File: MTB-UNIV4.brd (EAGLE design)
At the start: 106 x 67 mm, 138 parts, among them IC1 MEGA128-A, IC2 SN75176BP, IC3 MC7805CDTG, IC4 ULN2803A, IC5 ULN2803A, X1 CON-04-5.0CON-5MM, X2 CON-04-5.0CON-5MM, X3 1751316, X4 1751316, X5 1751316, X6 1751316

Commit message: Do not ground mount holes.
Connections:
- net GND: no longer H1.B3,2, H2.B3,2, H3.B3,2, H4.B3,2
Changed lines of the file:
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@@
 <?xml version="1.0" encoding="utf-8"?>
 <!DOCTYPE eagle SYSTEM "eagle.dtd">
-<eagle version="9.6.2">
+<eagle version="9.5.2">
 <drawing>
 <settings>
@@
 <setting verticaltext="up"/>
 </settings>
-<grid distance="0.5" unitdist="mm" unit="mm" style="lines" multiple="1" display="yes" altdistance="5" altunitdist="mil" altunit="mil"/>
+<grid distance="1.27" unitdist="mm" unit="mm" style="dots" multiple="2" display="no" altdistance="0.3175" altunitdist="mm" altunit="mm"/>
 <layers>
-<layer number="1" name="Top" color="4" fill="1" visible="yes" active="yes"/>
+<layer number="1" name="Top" color="3" fill="1" visible="yes" active="yes"/>
 <layer number="2" name="Route2" color="1" fill="3" visible="no" active="no"/>
 <layer number="3" name="Route3" color="4" fill="3" visible="no" active="no"/>
@@
 <layer number="14" name="Route14" color="1" fill="6" visible="no" active="no"/>
 <layer number="15" name="Route15" color="4" fill="6" visible="no" active="no"/>
-<layer number="16" name="Bottom" color="1" fill="1" visible="yes" active="yes"/>
+<layer number="16" name="Bottom" color="4" fill="1" visible="yes" active="yes"/>
 <layer number="17" name="Pads" color="2" fill="1" visible="yes" active="yes"/>
 <layer number="18" name="Vias" color="2" fill="1" visible="yes" active="yes"/>
@@
 <layer number="23" name="tOrigins" color="15" fill="1" visible="yes" active="yes"/>
 <layer number="24" name="bOrigins" color="15" fill="1" visible="yes" active="yes"/>
-<layer number="25" name="tNames" color="7" fill="1" visible="yes" active="yes"/>
-<layer number="26" name="bNames" color="7" fill="1" visible="yes" active="yes"/>
-<layer number="27" name="tValues" color="7" fill="1" visible="yes" active="yes"/>
+<layer number="25" name="tNames" color="7" fill="1" visible="no" active="yes"/>
+<layer number="26" name="bNames" color="7" fill="1" visible="no" active="yes"/>
+<layer number="27" name="tValues" color="7" fill="1" visible="no" active="yes"/>
 <layer number="28" name="bValues" color="7" fill="1" visible="no" active="yes"/>
 <layer number="29" name="tStop" color="7" fill="3" visible="no" active="yes"/>
@@
 <layer number="37" name="tTest" color="7" fill="1" visible="no" active="yes"/>
 <layer number="38" name="bTest" color="7" fill="1" visible="no" active="yes"/>
-<layer number="39" name="tKeepout" color="4" fill="11" visible="yes" active="yes"/>
-<layer number="40" name="bKeepout" color="1" fill="11" visible="yes" active="yes"/>
-<layer number="41" name="tRestrict" color="4" fill="10" visible="yes" active="yes"/>
-<layer number="42" name="bRestrict" color="1" fill="10" visible="yes" active="yes"/>
-<layer number="43" name="vRestrict" color="2" fill="10" visible="yes" active="yes"/>
+<layer number="39" name="tKeepout" color="4" fill="11" visible="no" active="yes"/>
+<layer number="40" name="bKeepout" color="1" fill="11" visible="no" active="yes"/>
+<layer number="41" name="tRestrict" color="4" fill="10" visible="no" active="yes"/>
+<layer number="42" name="bRestrict" color="1" fill="10" visible="no" active="yes"/>
+<layer number="43" name="vRestrict" color="2" fill="10" visible="no" active="yes"/>
 <layer number="44" name="Drills" color="7" fill="1" visible="no" active="yes"/>
-<layer number="45" name="Holes" color="7" fill="1" visible="yes" active="yes"/>
-<layer number="46" name="Milling" color="3" fill="1" visible="no" active="yes"/>
+<layer number="45" name="Holes" color="7" fill="1" visible="no" active="yes"/>
+<layer number="46" name="Milling" color="3" fill="1" visible="yes" active="yes"/>
 <layer number="47" name="Measures" color="7" fill="1" visible="no" active="yes"/>
-<layer number="48" name="Document" color="7" fill="1" visible="yes" active="yes"/>
+<layer number="48" name="Document" color="7" fill="1" visible="no" active="yes"/>
 <layer number="49" name="Reference" color="7" fill="1" visible="yes" active="yes"/>
 <layer number="50" name="dxf" color="7" fill="1" visible="no" active="yes"/>
@@
 <layer number="112" name="tSilk" color="7" fill="1" visible="no" active="yes"/>
 <layer number="113" name="ReferenceLS" color="7" fill="1" visible="no" active="no"/>
-<layer number="114" name="Badge_Outline" color="7" fill="1" visible="yes" active="yes"/>
-<layer number="115" name="ReferenceISLANDS" color="7" fill="1" visible="yes" active="yes"/>
-<layer number="116" name="Patch_BOT" color="9" fill="4" visible="no" active="yes"/>
+<layer number="114" name="Badge_Outline" color="7" fill="1" visible="no" active="yes"/>
+<layer number="115" name="ReferenceISLANDS" color="7" fill="1" visible="no" active="yes"/>
+<layer number="116" name="centerDrill" color="9" fill="4" visible="no" active="yes"/>
 <layer number="118" name="Rect_Pads" color="7" fill="1" visible="no" active="no"/>
 <layer number="121" name="_tsilk" color="7" fill="1" visible="no" active="yes"/>
@@
 <layer number="127" name="_tValues" color="7" fill="1" visible="no" active="yes"/>
 <layer number="128" name="_bValues" color="7" fill="1" visible="no" active="yes"/>
-<layer number="129" name="Mask" color="7" fill="1" visible="yes" active="yes"/>
+<layer number="129" name="Mask" color="7" fill="1" visible="no" active="yes"/>
 <layer number="131" name="tAdjust" color="7" fill="1" visible="no" active="yes"/>
 <layer number="132" name="bAdjust" color="7" fill="1" visible="no" active="yes"/>
@@
 <layer number="223" name="223bmp" color="24" fill="1" visible="no" active="no"/>
 <layer number="224" name="224bmp" color="25" fill="1" visible="no" active="no"/>
-<layer number="225" name="225bmp" color="7" fill="1" visible="yes" active="yes"/>
-<layer number="226" name="226bmp" color="7" fill="1" visible="yes" active="yes"/>
-<layer number="227" name="227bmp" color="7" fill="1" visible="yes" active="yes"/>
-<layer number="228" name="228bmp" color="7" fill="1" visible="yes" active="yes"/>
-<layer number="229" name="229bmp" color="7" fill="1" visible="yes" active="yes"/>
-<layer number="230" name="230bmp" color="7" fill="1" visible="yes" active="yes"/>
+<layer number="225" name="225bmp" color="7" fill="1" visible="no" active="yes"/>
+<layer number="226" name="226bmp" color="7" fill="1" visible="no" active="yes"/>
+<layer number="227" name="227bmp" color="7" fill="1" visible="no" active="yes"/>
+<layer number="228" name="228bmp" color="7" fill="1" visible="no" active="yes"/>
+<layer number="229" name="229bmp" color="7" fill="1" visible="no" active="yes"/>
+<layer number="230" name="230bmp" color="7" fill="1" visible="no" active="yes"/>
 <layer number="231" name="Eagle3D_PG1" color="7" fill="1" visible="no" active="no"/>
 <layer number="232" name="Eagle3D_PG2" color="7" fill="1" visible="no" active="no"/>
@@
 <layer number="251" name="SMDround" color="7" fill="1" visible="no" active="no"/>
 <layer number="254" name="cooling" color="7" fill="1" visible="no" active="yes"/>
-<layer number="255" name="routoute" color="7" fill="1" visible="yes" active="yes"/>
+<layer number="255" name="routoute" color="7" fill="1" visible="no" active="yes"/>
 </layers>
 <board>
@@
 <contactref element="R24" pad="1"/>
 <contactref element="TH5" pad="1"/>
-<contactref element="H4" pad="B3,2"/>
-<contactref element="H3" pad="B3,2"/>
-<contactref element="H2" pad="B3,2"/>
-<contactref element="H1" pad="B3,2"/>
 <contactref element="C2" pad="2"/>
 <contactref element="C1" pad="2"/>

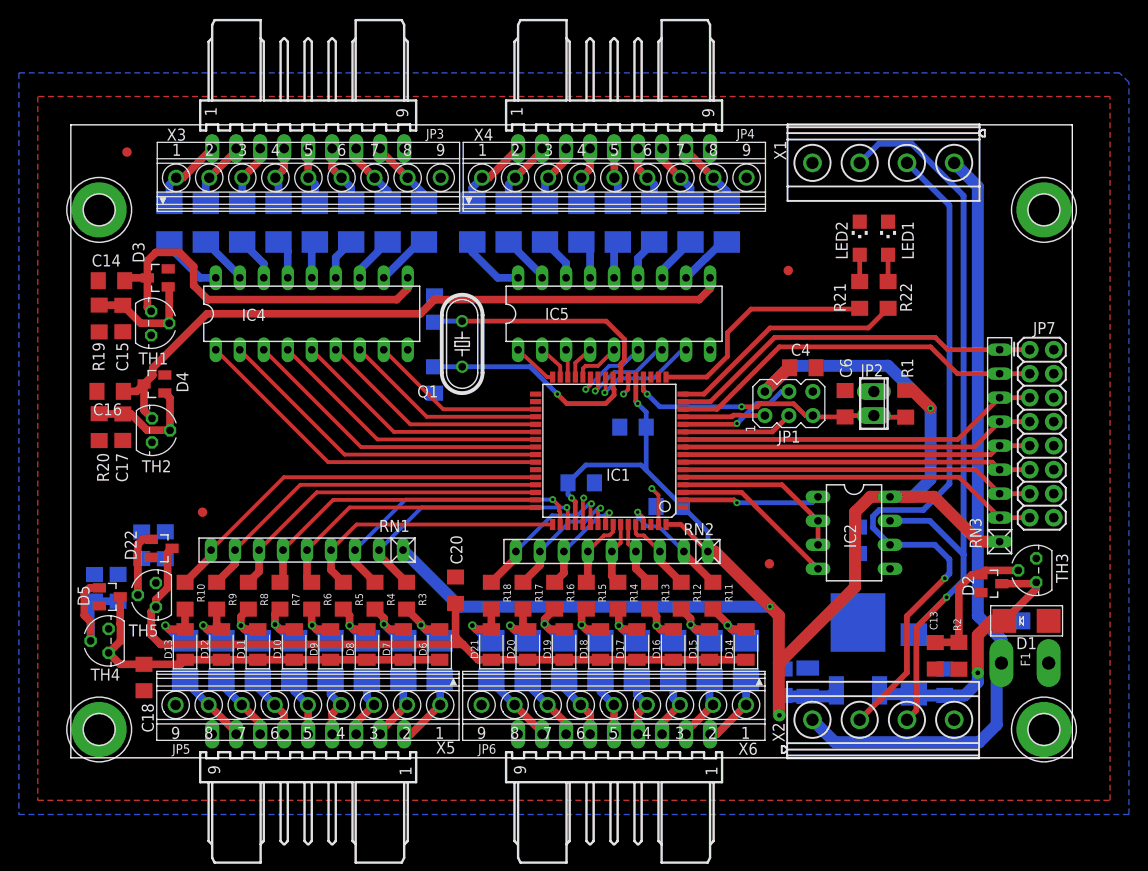
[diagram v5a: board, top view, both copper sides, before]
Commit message: Fit board to MTB-TTL size.
Make board smaller.
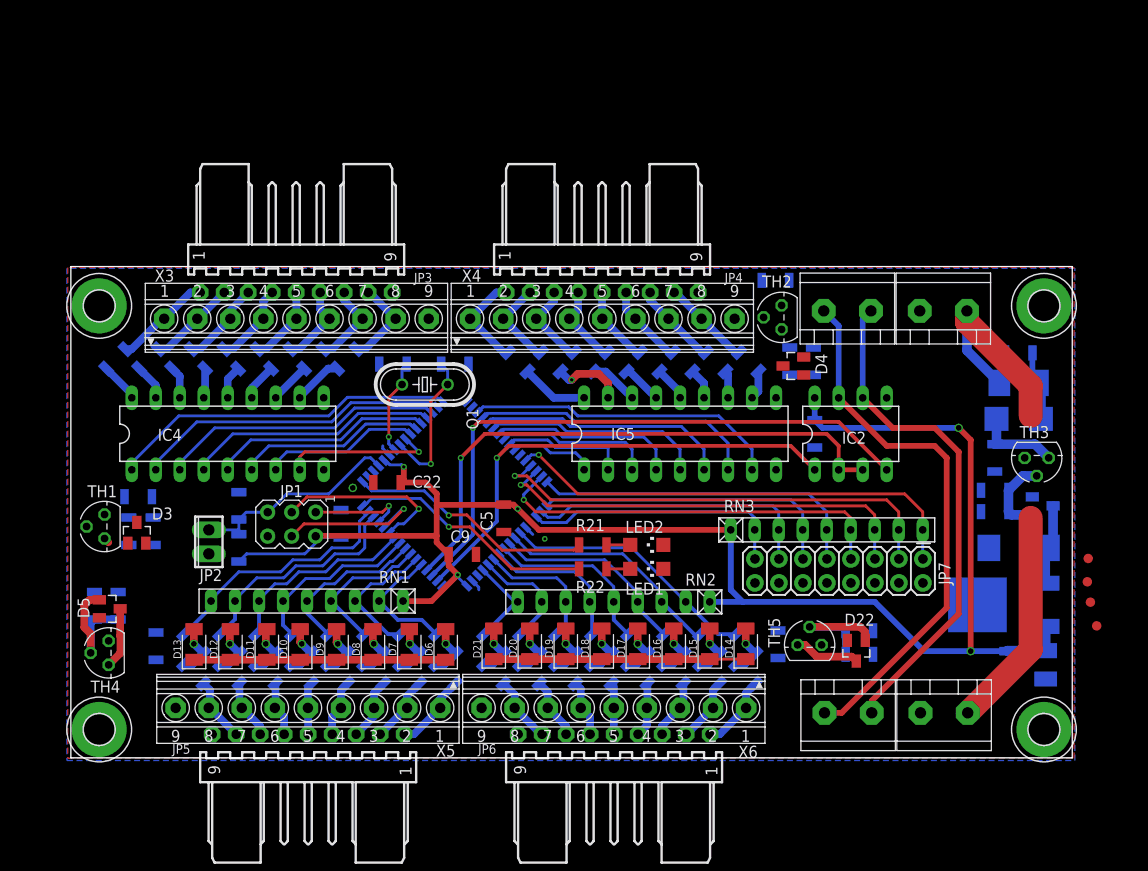
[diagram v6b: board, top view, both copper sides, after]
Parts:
- removed X2: CON-04-5.0CON-5MM, ElectroKrt:MKDSN1,5/4-5,00
- added X7, X8, X9: ARK500/2, con-malina:ARK500/2
- F1: device ElectroKrt:1X2-BIGPOGO-5MM -> adafruit_edited:1812
- F10, F11, F12, F13, F14, F15, F16, F17, F18, F19, F2, F20, F21, F22, F23, F24, F25, F26, F27, F28, F29, F3, F30, F31, F32, F33, F4, F5, F6, F7, F8, F9: device adafruit:1812 -> adafruit_edited:R1206S
- JP3, JP4, JP5, JP6: value 22-05-7098-09 -> 22-OCTHOLE-09; device con-molex:7395-09 -> con-molex:7395-09-OCTHOLE
- X1: value CON-04-5.0CON-5MM -> ARK500/2; device ElectroKrt:MKDSN1,5/4-5,00 -> con-malina:ARK500/2
- moved U$1 114.2 mm to (108.6, 14.0)
- moved U$4 94.5 mm to (107.9, 16.5)
- moved C21 76.5 mm to (83.5, 13.5), turned to 180 degrees
- moved R20 75.9 mm to (78.6, 42.0), flipped to the bottom
- moved R24 74.4 mm to (83.5, 11.0), turned to 0 degrees
- moved D22 74.3 mm to (83.1, 11.3), turned to 180 degrees
- moved R1 72.2 mm to (17.8, 22.2), flipped to the bottom, turned to 270 degrees
- moved JP2 71.9 mm to (14.6, 22.9), turned to 90 degrees
- moved C16 71.4 mm to (74.6, 50.5), flipped to the bottom
- moved C17 70.9 mm to (76.1, 42.0), flipped to the bottom
- moved TH5 69.4 mm to (78.2, 12.0), turned to 0 degrees
- moved TH2 67.7 mm to (75.2, 46.6), turned to 90 degrees
- moved D4 67.7 mm to (76.5, 41.5)
- moved C6 65.1 mm to (17.8, 26.7), flipped to the bottom
- moved X1 58.3 mm to (84.8, 4.76)
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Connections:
- net +12V: now also F1.1, X7.2, X9.1; no longer F1.P$1, X1.1, X2.1
- net ADDR-1: now also IC1.44; no longer IC1.15
- net ADDR-2: now also IC1.45; no longer IC1.14
- net ADDR-3: now also IC1.46; no longer IC1.10
- net ADDR-4: now also IC1.47; no longer IC1.9
- net ADDR-5: now also IC1.48; no longer IC1.8
- net ADDR-6: now also IC1.49; no longer IC1.7
- net ADDR-7: now also IC1.50; no longer IC1.6
- net ADDR-8: now also IC1.51; no longer IC1.5
- net D-IN(A)1: now also IC1.5; no longer IC1.51
- net D-IN(A)2: now also IC1.6; no longer IC1.50
- net D-IN(A)3: now also IC1.7; no longer IC1.49
- net D-IN(A)4: now also IC1.8; no longer IC1.48
- net D-IN(A)5: now also IC1.9; no longer IC1.47
- net D-IN(A)6: now also IC1.10; no longer IC1.46
- net D-IN(A)7: now also IC1.14; no longer IC1.45
- net D-IN(A)8: now also IC1.15; no longer IC1.44
- net D-IN(B)1: now also IC1.54; no longer IC1.61
- net D-IN(B)2: now also IC1.55; no longer IC1.60
- net D-IN(B)3: now also IC1.56; no longer IC1.59
- net D-IN(B)4: now also IC1.57; no longer IC1.58
- net D-IN(B)5: now also IC1.58; no longer IC1.57
- net D-IN(B)6: now also IC1.59; no longer IC1.56
- net D-IN(B)7: now also IC1.60; no longer IC1.55
- net D-IN(B)8: now also IC1.61; no longer IC1.54
- net D-OUT(A)1: now also IC1.32; no longer IC1.42
- net D-OUT(A)2: now also IC1.31; no longer IC1.41
- net D-OUT(A)3: now also IC1.30; no longer IC1.40
- net D-OUT(A)4: now also IC1.29; no longer IC1.39
- net D-OUT(A)5: now also IC1.28; no longer IC1.38
- net D-OUT(A)6: now also IC1.27; no longer IC1.37
- net D-OUT(A)7: now also IC1.26; no longer IC1.36
- net D-OUT(A)8: now also IC1.25; no longer IC1.35
- net D-OUT(B)1: now also IC1.42; no longer IC1.32
- net D-OUT(B)2: now also IC1.41; no longer IC1.31
- net D-OUT(B)3: now also IC1.40; no longer IC1.30
- net D-OUT(B)4: now also IC1.39; no longer IC1.29
- net D-OUT(B)5: now also IC1.38; no longer IC1.28
- net D-OUT(B)6: now also IC1.37; no longer IC1.27
- net D-OUT(B)7: now also IC1.36; no longer IC1.26
- net D-OUT(B)8: now also IC1.35; no longer IC1.25
- net GND: now also X7.1, X9.2; no longer X1.4, X2.4
- net N$58: now also F1.2; no longer F1.P$2
- net RS-A: now also X1.1, X8.2; no longer X1.2, X2.2
- net RS-B: now also X1.2, X8.1; no longer X1.3, X2.3
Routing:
- net N$11: track 72.2 -> 0.00 mm
- net RS-D: track 17.6 -> 63.6 mm, vias 0 -> 1
- net N$80: track 78.8 -> 33.6 mm
- net RS-E: track 18.4 -> 60.0 mm, vias 0 -> 1
- net N$37: track 40.8 -> 0.57 mm
- net +12V: track 83.0 -> 46.3 mm
- net RS-R: track 14.7 -> 50.8 mm
- net RS-B: track 81.4 -> 57.4 mm, vias 1 -> 0
- net RS-A: track 77.0 -> 53.5 mm, vias 1 -> 0
- net D-OUT(B)8: track 12.2 -> 33.3 mm, vias 1 -> 0
- net D-OUT(B)7: track 10.5 -> 30.3 mm, vias 1 -> 0
- net D-OUT(B)5: track 5.03 -> 23.2 mm
- net +5V: track 194.9 -> 176.8 mm
- net D-OUT(B)6: track 8.78 -> 26.6 mm, vias 1 -> 0
- net D-OUT(B)4: track 3.60 -> 19.9 mm
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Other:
- board size 106 x 67 mm -> 106 x 52 mm

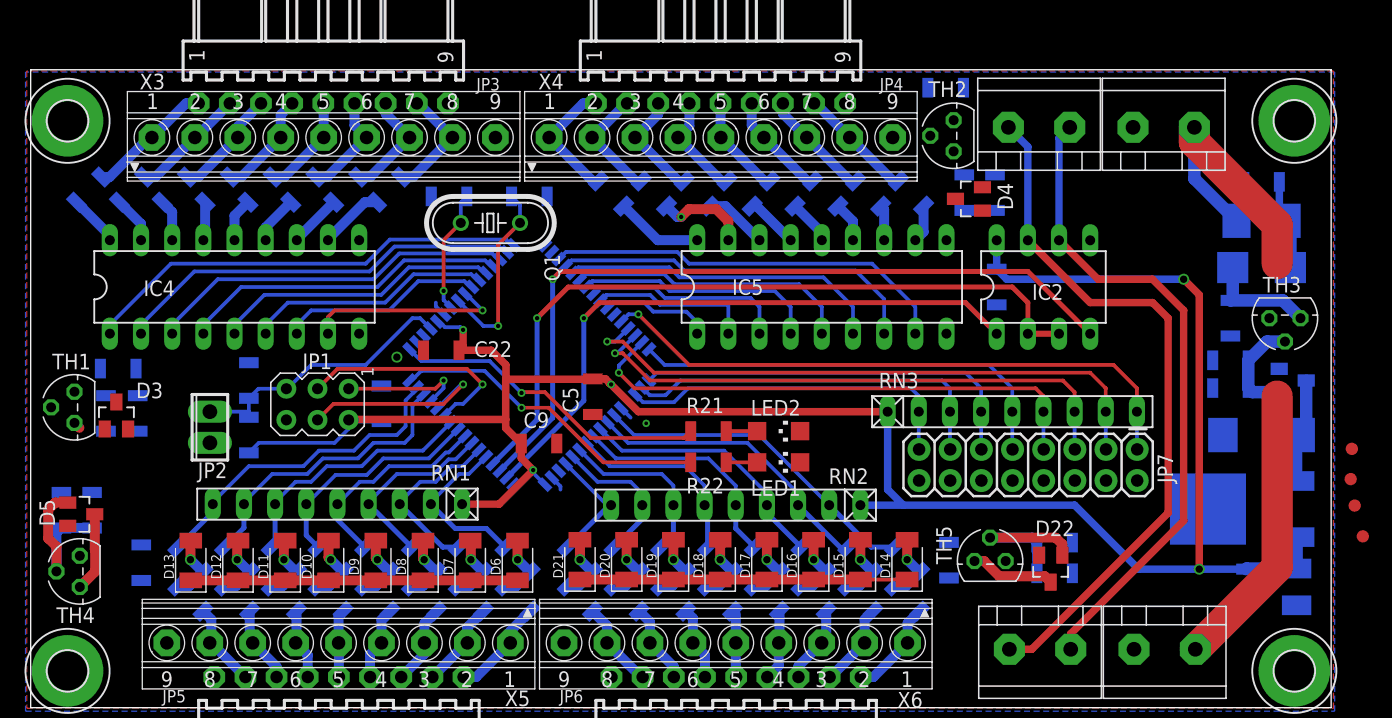
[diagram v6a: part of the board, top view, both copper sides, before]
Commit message: TTL-SIZE: everything routed.
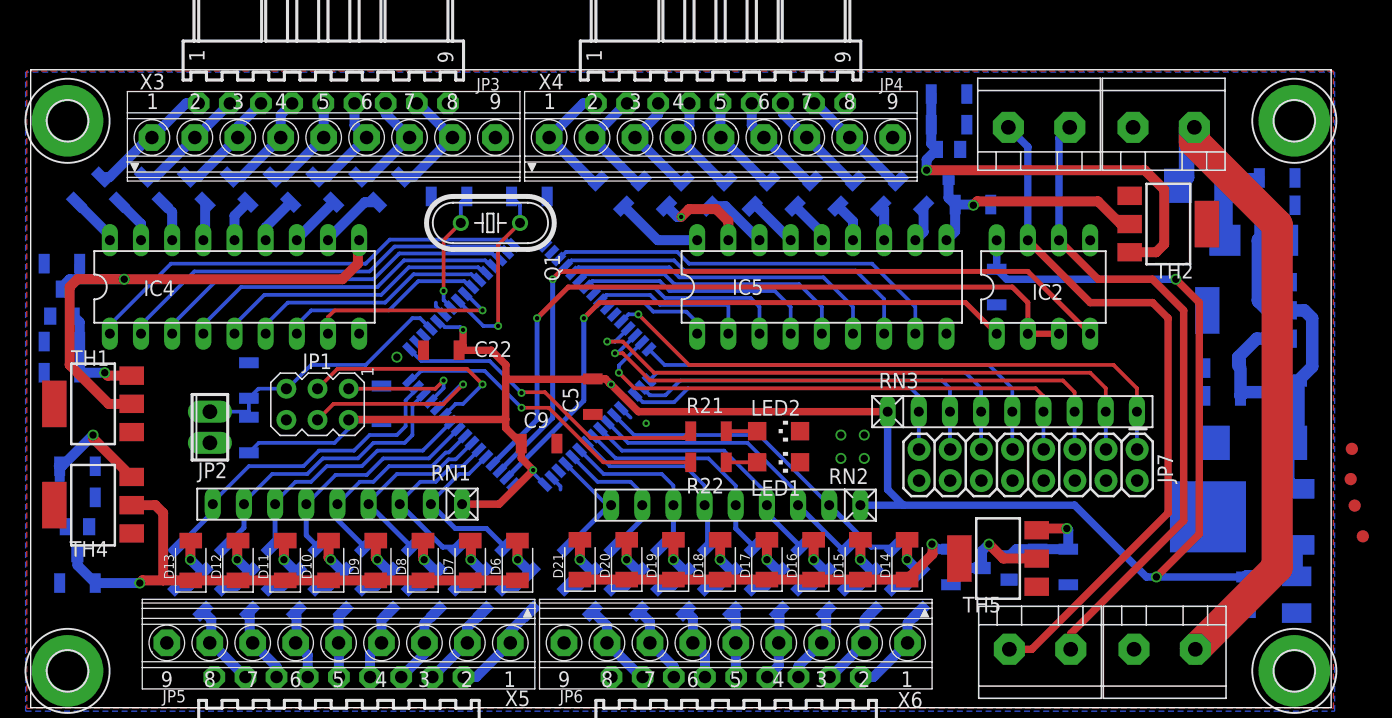
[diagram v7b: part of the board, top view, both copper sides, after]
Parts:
- TH1, TH2, TH3, TH4, TH5: value MCR100 -> BT148; device ElectroKrt:TO92 -> ElectroKrt:SOT223
- moved TH2 18.9 mm to (92.7, 39.4), turned to 270 degrees
- moved D3 10.2 mm to (2.54, 33.0), flipped to the bottom
- moved C7 9.96 mm to (101.6, 41.0), turned to 180 degrees
- moved C16 9.78 mm to (76.8, 41.0)
- moved C14 9.71 mm to (2.54, 36.2), turned to 0 degrees
- moved R20 8.87 mm to (74.9, 50.0), turned to 0 degrees
- moved R19 7.01 mm to (2.54, 27.3), turned to 180 degrees
- moved C15 6.87 mm to (2.54, 29.8), turned to 0 degrees
- moved C17 5.68 mm to (74.9, 47.5), turned to 180 degrees
- moved F1 5.55 mm to (95.6, 42.5)
- moved TH4 5.51 mm to (5.08, 16.5)
- moved C18 5.46 mm to (3.81, 10.2), turned to 0 degrees
- moved D22 4.50 mm to (78.6, 11.4), flipped to the bottom, turned to 270 degrees
- moved C19 3.82 mm to (3.81, 19.7), turned to 0 degrees
- moved D4 3.37 mm to (74.8, 44.4), flipped to the bottom, turned to 180 degrees
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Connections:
- net N$11: now also TH2.2; no longer TH2.3
- net N$13: now also TH3.2; no longer TH3.3
- net N$37: now also TH1.2; no longer TH1.3
- net N$46: now also TH1.3; no longer TH1.2
- net N$56: now also TH2.3; no longer TH2.2
- net N$57: now also TH3.3; no longer TH3.2
- net N$70: now also TH4.2; no longer TH4.3
- net N$71: now also TH4.3; no longer TH4.2
- net N$80: now also TH5.2; no longer TH5.3
- net N$81: now also TH5.3; no longer TH5.2
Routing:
- net N$37: track 0.57 -> 45.8 mm, vias 0 -> 1
- net N$56: track 0.00 -> 34.3 mm, vias 0 -> 1
- net N$11: track 0.00 -> 20.9 mm, vias 0 -> 1
- net N$70: track 33.2 -> 45.8 mm, vias 0 -> 1
- net N$13: track 17.6 -> 29.5 mm
- net N$46: track 0.00 -> 9.16 mm, vias 0 -> 1
- net N$80: track 33.6 -> 41.9 mm, vias 0 -> 2
- net +12V: track 46.3 -> 53.4 mm
- net N$81: track 13.6 -> 9.32 mm, vias 0 -> 1
- net +5V: track 176.8 -> 178.7 mm
- net N$57: track 8.55 -> 10.3 mm
- net N$71: track 13.4 -> 13.8 mm, vias 0 -> 1
- net GND: vias 2 -> 6
